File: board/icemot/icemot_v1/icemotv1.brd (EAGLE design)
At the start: 160 x 100 mm, 20 parts, among them U1 ICE40HX4K, U2 EFM32WG332FXXX-QFP64, Y1 48MHz

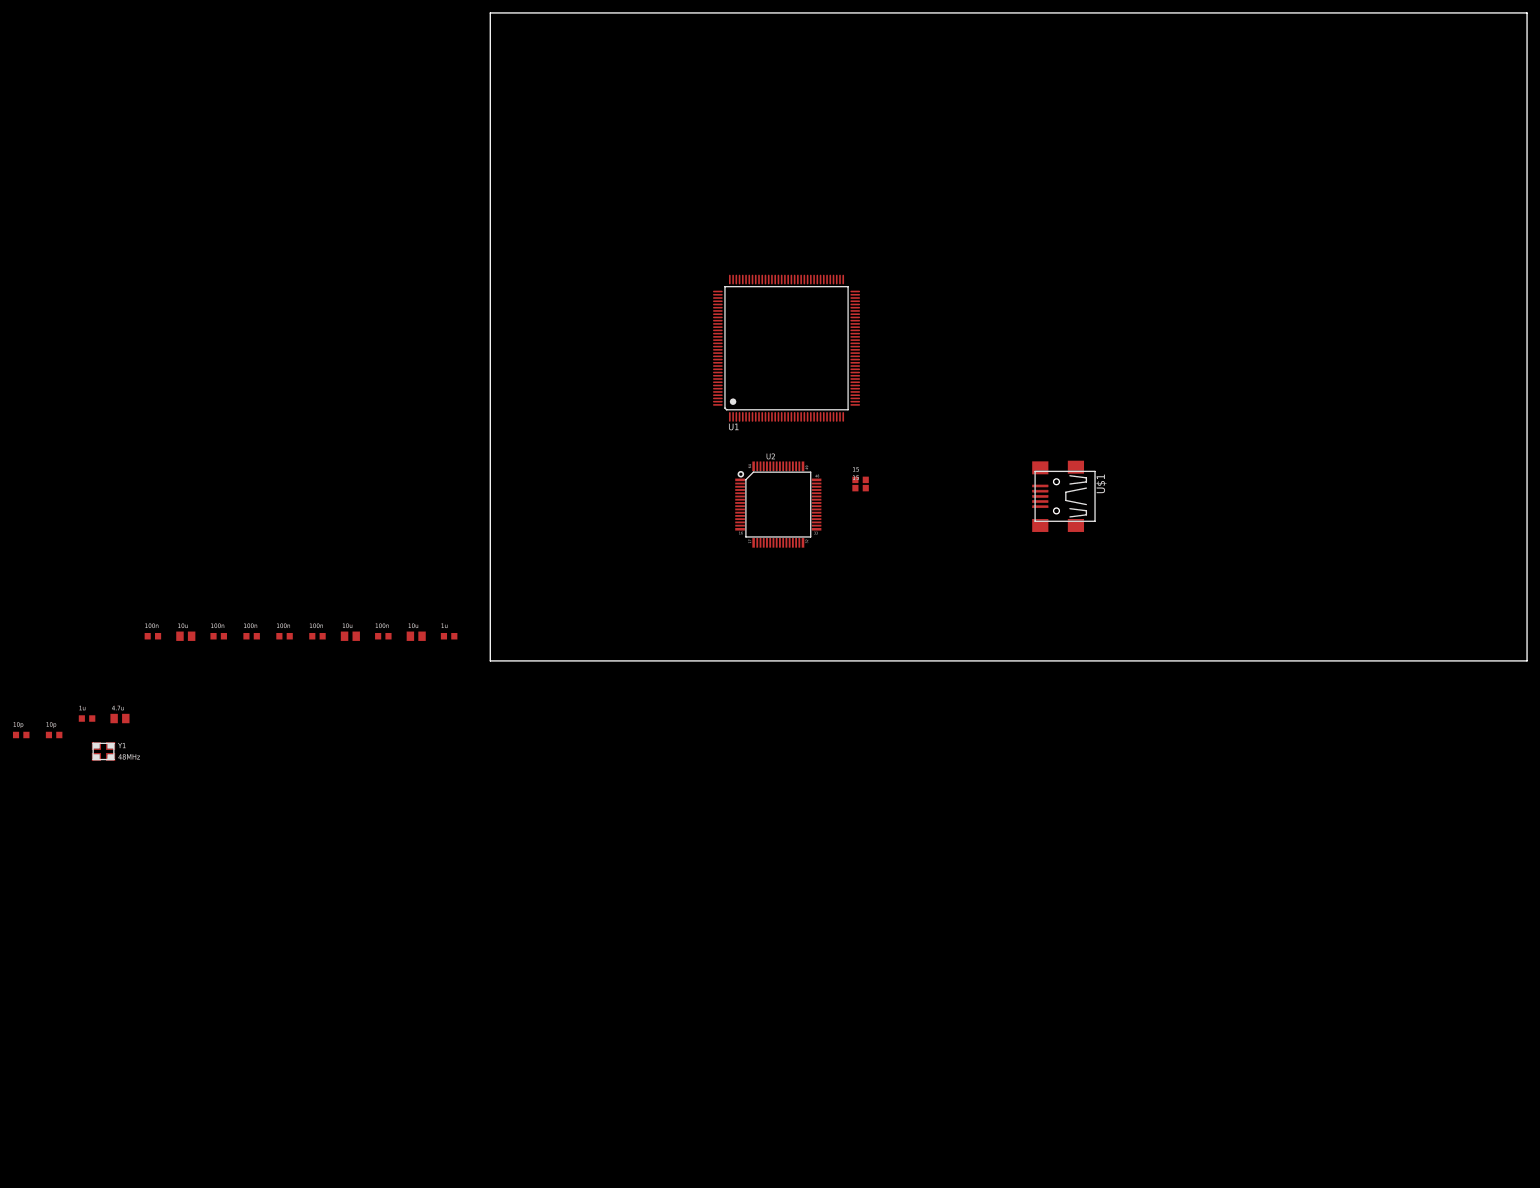
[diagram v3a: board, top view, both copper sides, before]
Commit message: need to add interface to motor
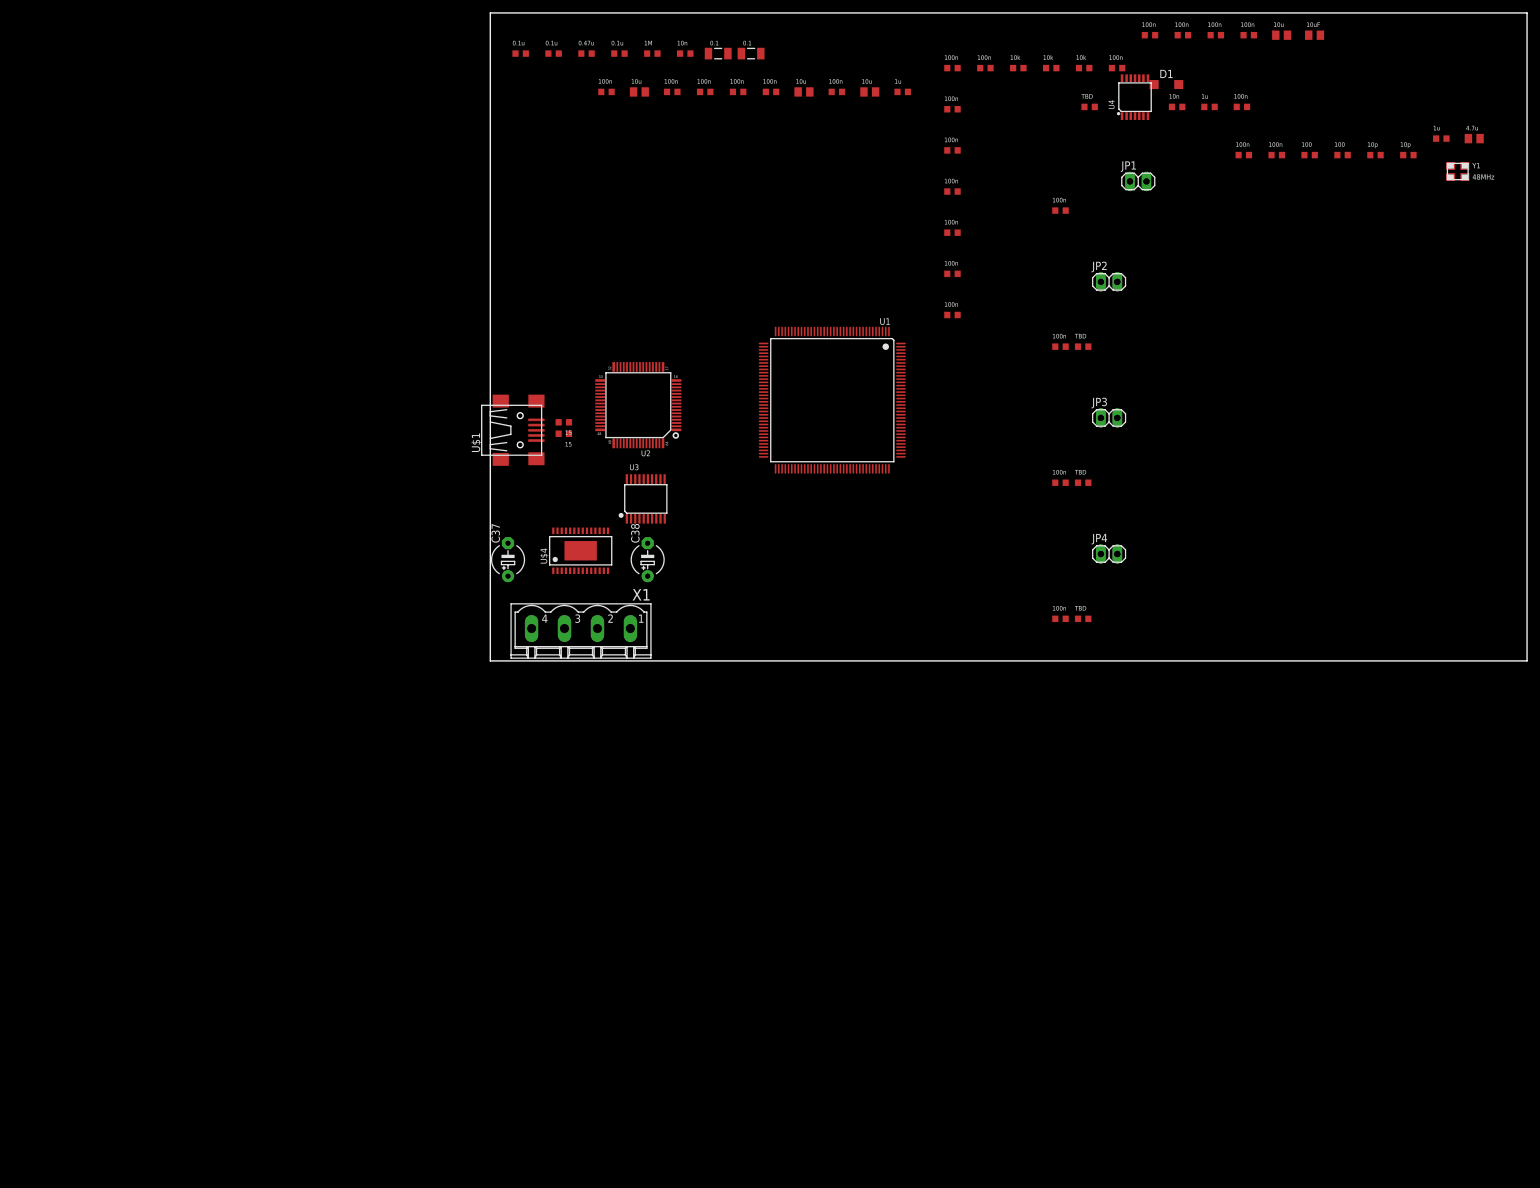
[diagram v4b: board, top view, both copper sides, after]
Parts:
- added C15, C16, C19, C20, C21, C22, C23, C24, C25, C26, C27, C28, C29, C30, C31, C39, C42, C43, C44, C45: 100n, standard_passive:R0603
- added C17: 10uF, standard_passive:R0805
- added C18: 10u, standard_passive:R0805
- added C32, C41: 10n, standard_passive:R0603
- added C33, C35, C36: 0.1u, standard_passive:R0603
- added C34: 0.47u, standard_passive:R0603
- added C37, C38: (no value), rcl:E5-5
- added C40: 1u, standard_passive:R0603
- added D1: (no value), diode:SOD123
- added JP1, JP2, JP3, JP4: (no value), pinhead:1X02
- added R10: 1M, standard_passive:R0603
- added R11, R12, R13, R14: TBD, standard_passive:R0603
- added R3, R4: 100, standard_passive:R0603
- added R5, R6, R7: 10k, standard_passive:R0603
- added R8, R9: 0.1, standard_passive:R1206
- added U$4: DRV8825PWP, motor_drivers:TSSOP-28
- added U3: MAX5723/4/5, dac:TSSOP20-0.65-6.5X4.4MM
- added U4: TLV4379, opamp:TSSOP14-0.65-5X4.4MM
- added X1: MSTBV4, con-phoenix-508:MSTBV4
- moved C11 227.4 mm to (151.8, 80.6)
- moved C12 227.4 mm to (146.8, 80.6)
- moved C13 227.4 mm to (141.7, 78.1)
- moved C14 227.4 mm to (136.6, 78.1)
- moved Y1 227.4 mm to (149.3, 75.5)
- moved C1 109.3 mm to (63.6, 87.8)
- moved C10 109.3 mm to (17.9, 87.8)
- moved C2 109.3 mm to (58.6, 87.8)
- moved C3 109.3 mm to (53.5, 87.8)
- moved C4 109.3 mm to (48.4, 87.8)
- moved C5 109.3 mm to (43.3, 87.8)
- moved C6 109.3 mm to (38.2, 87.8)
- moved C7 109.3 mm to (33.2, 87.8)
- moved C8 109.3 mm to (28.1, 87.8)
- moved C9 109.3 mm to (23.0, 87.8)
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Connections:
- removed net PLLGND: U1.127, U1.53
- removed net PLLVCC: U1.126, U1.54
- removed net SPI_VCC: U1.72
- removed net VCCIO2: U1.46, U1.57
- removed net VPP_2V5: U1.108
- new net CDONE: R6.1, U1.65
- new net CONF_CS: R5.2, U1.71, U2.62
- new net CONF_MISO: U1.67, U2.60, U3.12
- new net CONF_MOSI: U1.68, U2.59, U3.13
- new net CONF_SCK: U1.70, U2.61, U3.14
- new net CRESET: R7.1, U1.66
- new net DAC_CS: U2.63, U3.15
- new net MOT1_REF: U3.2
- new net N$10: C16.1, C18.1, R4.2, U1.54
- new net N$11: C15.1, C17.1, R3.2, U1.126
- new net N$12: C15.2, C17.2, U1.127
- new net N$13: C16.2, C18.2, U1.53
- new net N$14: D1.C, U1.108
- new net N$15: U2.64
- new net N$16: R9.2, U$4.6
- new net N$17: R8.2, U$4.9
- new net N$18: C32.1, U$4.1
- new net N$19: C32.2, U$4.2
- new net N$20: C33.1, R10.1, U$4.3
- new net N$21: U$4.12, U$4.13
- new net N$22: U$4.16, U$4.17
- new net N$23: U$4.18
- new net N$24: U$4.19
- new net N$25: U$4.20
- new net N$26: U$4.22
- new net N$27: U$4.21
- new net N$29: U$4.5, X1.4
- new net N$30: U$4.7, X1.3
- new net N$31: U$4.8, X1.2
- new net N$32: U$4.10, X1.1
- new net N$34: U3.3
- new net N$35: U3.4
- new net N$36: U3.5
- new net N$37: U3.6
- new net N$38: U3.7
- new net N$39: U3.8
- new net N$40: U3.9
- new net T1_AMP: U2.31, U4.1, U4.2
- new net T1_IN: C42.1, JP1.1, R11.2, U4.3
- new net T2_AMP: U2.32, U4.6, U4.7
- new net T2_IN: C43.1, JP2.1, R12.2, U4.5
- new net T3_AMP: U2.33, U4.8, U4.9
- new net T3_IN: C44.1, JP3.1, R13.2, U4.10
- new net T4_AMP: U2.34, U4.13, U4.14
- new net T4_IN: C45.1, JP4.1, R14.2, U4.12
- net +1V2: now also C19.1, C20.1, C21.1, C22.1, C33.2, C35.1, C36.1, C37.+, C38.+, R10.2, R3.1, R4.1, U$4.11, U$4.4
- net +3V3: now also C23.1, C24.1, C25.1, C26.1, C27.1, C28.1, C29.1, C30.1, C31.1, C34.2, C39.1, C40.1, C41.1, D1.A, JP1.2, JP2.2, JP3.2, JP4.2, R6.2, R7.2, U$4.15, U$4.24, U$4.25, U$4.26, U1.46, U1.57, U1.72, U3.10, U3.11, U3.17, U3.18, U4.4
- net GND: now also C19.2, C20.2, C21.2, C22.2, C23.2, C24.2, C25.2, C26.2, C27.2, C28.2, C29.2, C30.2, C31.2, C34.1, C35.2, C36.2, C37.-, C38.-, C39.2, C40.2, C41.2, C42.2, C43.2, C44.2, C45.2, R11.1, R12.1, R13.1, R14.1, R5.1, R8.1, R9.1, U$4.14, U$4.28, U$4.29, U3.19, U3.20, U4.11

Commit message: added oscillator, clock to be routed on GBin
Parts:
- added C46: 0.47u, standard_passive:R0603
- added C47, C48: 0.1u, standard_passive:R0603
- added U$6: 3.2X2.5X2.0-TCXO, oscillators:3.2X2.5X2.0-TCXO
- moved Y1 127.0 mm to (24.1, 54.1), turned to 180 degrees
- moved C13 122.5 mm to (21.5, 54.2), turned to 90 degrees
- moved C14 112.4 mm to (26.7, 54.2), turned to 90 degrees
- moved R8 83.8 mm to (22.5, 11.8), turned to 90 degrees
- moved R9 83.2 mm to (20.4, 11.8), turned to 90 degrees
- moved C36 82.7 mm to (25.6, 13.8)
- moved C35 82.3 mm to (17.2, 11.8), turned to 180 degrees
- moved R10 81.0 mm to (17.2, 13.1)
- moved C33 79.3 mm to (17.2, 14.4)
- moved C32 77.1 mm to (15.6, 18.0), turned to 90 degrees
- moved U3 16.0 mm to (8.50, 29.0), turned to 90 degrees
- moved C37 10.2 mm to (12.7, 13.6)
- moved U$4 7.91 mm to (21.4, 19.5)
- moved X1 7.52 mm to (21.5, 4.50), turned to 0 degrees
- moved C38 6.32 mm to (30.3, 13.6)
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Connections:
- removed net MOT1_REF: U3.2
- removed net N$21: U$4.12, U$4.13
- new net +40V: C33.2, C35.1, C36.1, C37.+, C38.+, R10.2, U$4.11, U$4.4
- new net +40V1: C47.1, C48.1
- new net MOT1_VREF: C46.1, U$4.12, U$4.13, U3.2
- new net VDD: U$6.4
- net +1V2: no longer C33.2, C35.1, C36.1, C37.+, C38.+, R10.2, U$4.11, U$4.4
- net GND: now also C46.2, C47.2, C48.2, U$6.2
- net N$29: now also X1.1; no longer X1.4
- net N$30: now also X1.2; no longer X1.3
- net N$31: now also X1.3; no longer X1.2
- net N$32: now also X1.4; no longer X1.1

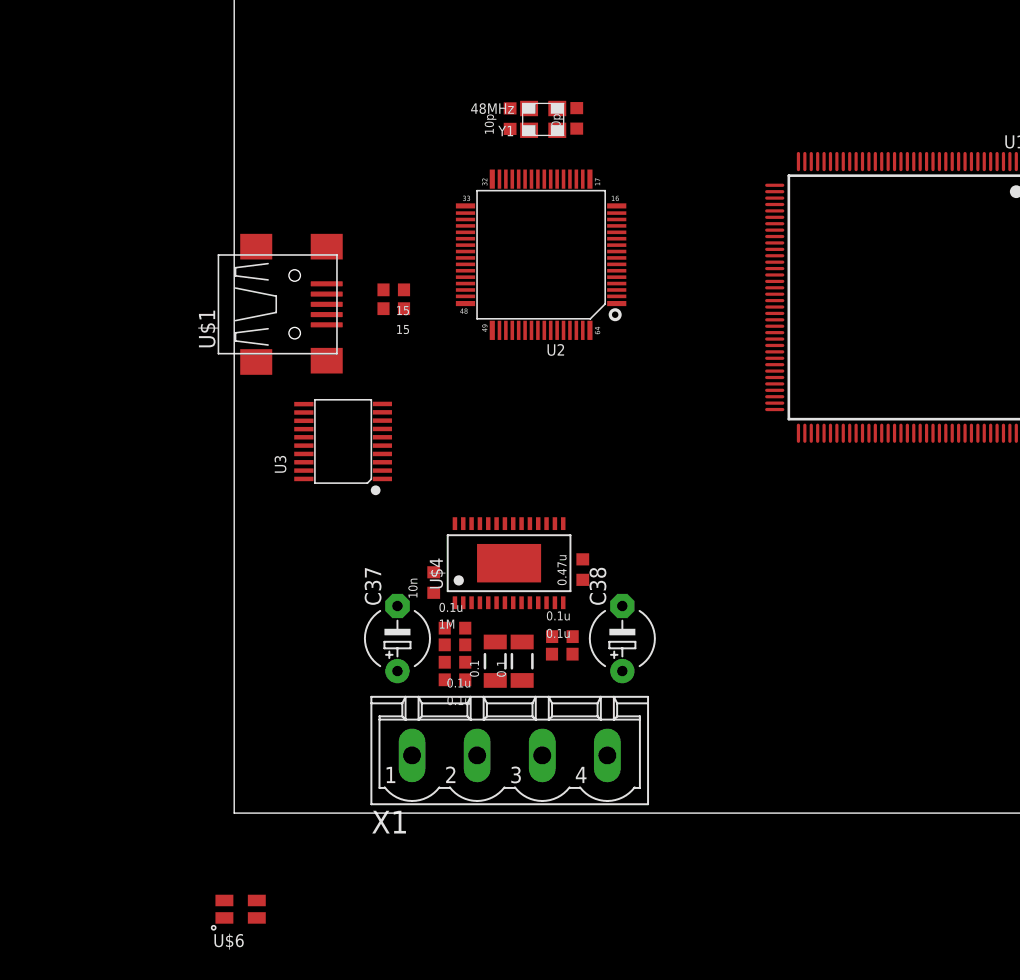
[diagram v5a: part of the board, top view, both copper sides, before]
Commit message: added res on decay
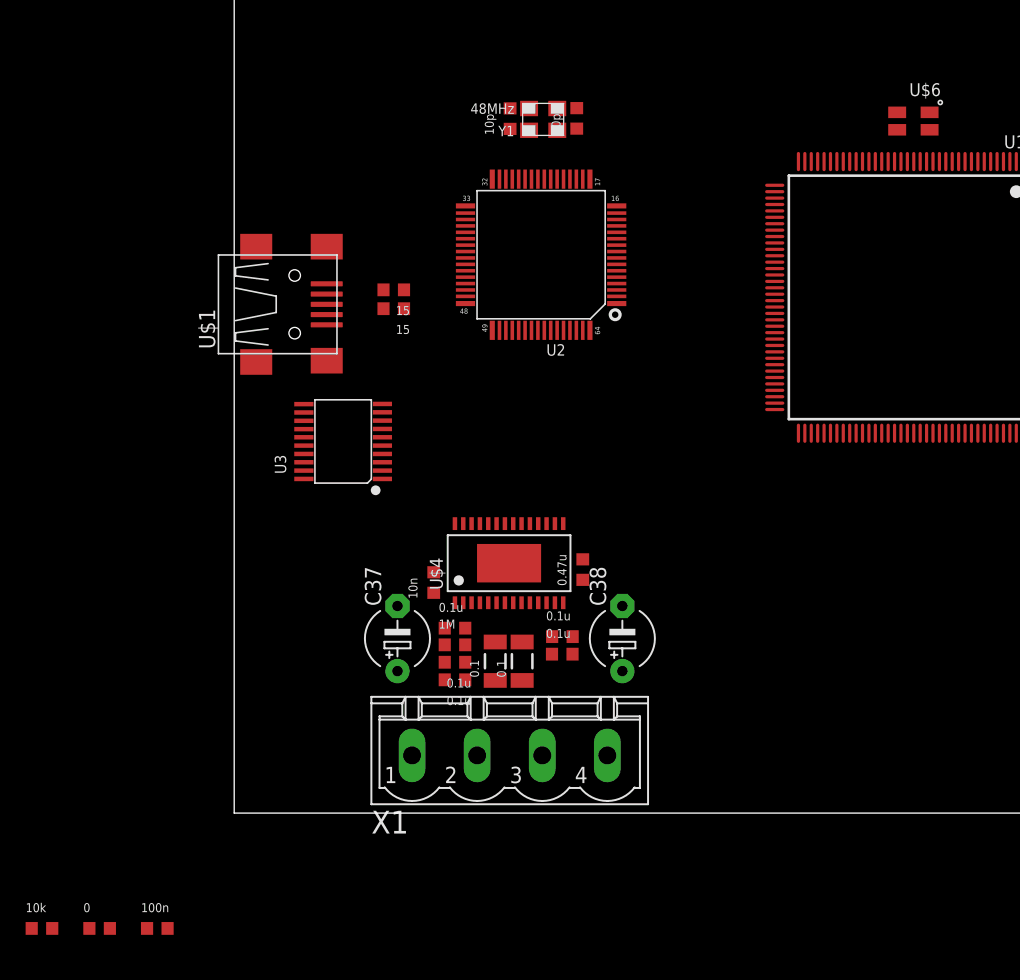
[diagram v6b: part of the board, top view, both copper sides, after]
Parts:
- added C49: 100n, standard_passive:R0603
- added R15: 0, standard_passive:R0603
- added R16: 10k, standard_passive:R0603
- moved U$6 80.9 mm to (53.0, 54.0), turned to 180 degrees
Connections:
- removed net N$22: U$4.16, U$4.17
- removed net N$23: U$4.18
- removed net N$25: U$4.20
- removed net N$26: U$4.22
- removed net N$27: U$4.21
- removed net VDD: U$6.4
- new net MOT1_DIR: U$4.20, U1.60
- new net MOT1_EN: U$4.21, U1.61
- new net MOT1_FAULT: R16.1, U$4.18, U1.62
- new net MOT1_RST: U$4.16, U$4.17, U1.55
- new net MOT1_STEP: U$4.22, U1.56
- new net N$21: U$6.3, U1.21
- net +3V3: now also C49.1, R15.1, R16.2, U$6.4
- net GND: now also C49.2
- net N$24: now also R15.2
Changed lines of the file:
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@@
 <element name="C47" library="standard_passive" package="R0603" value="0.1u" x="17.23" y="10.4" rot="R180"/>
 <element name="C48" library="standard_passive" package="R0603" value="0.1u" x="25.6" y="12.4"/>
-<element name="U$6" library="oscillators" package="3.2X2.5X2.0-TCXO" value="3.2X2.5X2.0-TCXO" x="0.5" y="-7.5"/>
+<element name="U$6" library="oscillators" package="3.2X2.5X2.0-TCXO" value="3.2X2.5X2.0-TCXO" x="53" y="54" rot="R180"/>
+<element name="C49" library="standard_passive" package="R0603" value="100n" x="-6" y="-9"/>
+<element name="R15" library="standard_passive" package="R0603" value="0" x="-10.5" y="-9"/>
+<element name="R16" library="standard_passive" package="R0603" value="10k" x="-15" y="-9"/>
 </elements>
 <signals>
@@
 <contactref element="C47" pad="2"/>
 <contactref element="U$6" pad="2"/>
+<contactref element="C49" pad="2"/>
 <wire x1="145.97" y1="80.61" x2="152.75" y2="80.61" width="0" layer="19" extent="1-1"/>
 <wire x1="116.8" y1="85.5" x2="145.97" y2="80.61" width="0" layer="19" extent="1-1"/>
@@
 <wire x1="90.7" y1="6.5" x2="90.7" y2="27.5" width="0" layer="19" extent="1-1"/>
 <wire x1="88.8" y1="6.5" x2="90.7" y2="6.5" width="0" layer="19" extent="1-1"/>
-<wire x1="1.765" y1="-8.18" x2="16.43" y2="10.4" width="0" layer="19" extent="1-1"/>
+<wire x1="51.735" y1="54.68" x2="16.43" y2="10.4" width="0" layer="19" extent="1-1"/>
+<wire x1="-5.2" y1="-9" x2="51.735" y2="54.68" width="0" layer="19" extent="1-1"/>
 </signal>
 <signal name="VPP_FAST">
@@
 <contactref element="JP3" pad="2"/>
 <contactref element="JP4" pad="2"/>
+<contactref element="C49" pad="1"/>
+<contactref element="U$6" pad="4"/>
+<contactref element="R15" pad="1"/>
+<contactref element="R16" pad="2"/>
 <wire x1="110.2" y1="85.5" x2="115.2" y2="85.5" width="0" layer="19" extent="1-1"/>
 <wire x1="105.2" y1="85.5" x2="110.2" y2="85.5" width="0" layer="19" extent="1-1"/>
@@
 <wire x1="19.825" y1="22.5875" x2="19.175" y2="22.5875" width="0" layer="19" extent="1-1"/>
 <wire x1="25.675" y1="22.5875" x2="19.825" y2="22.5875" width="0" layer="19" extent="1-1"/>
+<wire x1="54.265" y1="53.32" x2="5.435" y2="27.375" width="0" layer="19" extent="1-1"/>
+<wire x1="-6.8" y1="-9" x2="54.265" y2="53.32" width="0" layer="19" extent="1-1"/>
+<wire x1="-11.3" y1="-9" x2="-6.8" y2="-9" width="0" layer="19" extent="1-1"/>
+<wire x1="-14.2" y1="-9" x2="-11.3" y2="-9" width="0" layer="19" extent="1-1"/>
 </signal>
 <signal name="N$1">
@@
 <wire x1="11.565" y1="26.725" x2="24.375" y2="16.4125" width="0" layer="19" extent="1-1"/>
 </signal>
-<signal name="N$22">
+<signal name="MOT1_RST">
 <contactref element="U$4" pad="16"/>
 <contactref element="U$4" pad="17"/>
+<contactref element="U1" pad="55"/>
+<wire x1="25.025" y1="22.5875" x2="42.18" y2="39.99" width="0" layer="19" extent="1-1"/>
 <wire x1="24.375" y1="22.5875" x2="25.025" y2="22.5875" width="0" layer="19" extent="1-1"/>
 </signal>
-<signal name="N$23">
+<signal name="MOT1_FAULT">
 <contactref element="U$4" pad="18"/>
-</signal>
-<signal name="N$24">
-<contactref element="U$4" pad="19"/>
-</signal>
-<signal name="N$25">
+<contactref element="R16" pad="1"/>
+<contactref element="U1" pad="62"/>
+<wire x1="23.725" y1="22.5875" x2="42.18" y2="36.49" width="0" layer="19" extent="1-1"/>
+<wire x1="-15.8" y1="-9" x2="23.725" y2="22.5875" width="0" layer="19" extent="1-1"/>
+</signal>
+<signal name="MOT1_DIR">
 <contactref element="U$4" pad="20"/>
-</signal>
-<signal name="N$26">
+<contactref element="U1" pad="60"/>
+<wire x1="22.425" y1="22.5875" x2="42.18" y2="37.49" width="0" layer="19" extent="1-1"/>
+</signal>
+<signal name="MOT1_STEP">
 <contactref element="U$4" pad="22"/>
-</signal>
-<signal name="N$27">
+<contactref element="U1" pad="56"/>
+<wire x1="21.125" y1="22.5875" x2="42.18" y2="39.49" width="0" layer="19" extent="1-1"/>
+</signal>
+<signal name="MOT1_EN">
 <contactref element="U$4" pad="21"/>
+<contactref element="U1" pad="61"/>
+<wire x1="21.775" y1="22.5875" x2="42.18" y2="36.99" width="0" layer="19" extent="1-1"/>
 </signal>
 <signal name="N$29">
@@
 <wire x1="18.03" y1="10.4" x2="24.8" y2="12.4" width="0" layer="19" extent="1-1"/>
 </signal>
-<signal name="VDD">
-<contactref element="U$6" pad="4"/>
+<signal name="N$21">
+<contactref element="U$6" pad="3"/>
+<contactref element="U1" pad="21"/>
+<wire x1="51.735" y1="53.32" x2="51.53" y2="50.84" width="0" layer="19" extent="1-1"/>
+</signal>
+<signal name="N$24">
+<contactref element="R15" pad="2"/>
+<contactref element="U$4" pad="19"/>
+<wire x1="-9.7" y1="-9" x2="23.075" y2="22.5875" width="0" layer="19" extent="1-1"/>
 </signal>
 </signals>
